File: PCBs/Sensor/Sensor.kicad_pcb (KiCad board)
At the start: 2 copper layers, 35 x 45 mm, 12 parts, among them J1 Conn_01x04_Pin, J2 RJ45, J3 RJ45, J4 RJ45, U1 ATtiny85-20P

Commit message: fixed pcb
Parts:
- JP1: value Jumper_2_Bridged -> Jumper_2_Open; footprint Jumper:SolderJumper-2_P1.3mm_Bridged_RoundedPad1.0x1.5mm -> Jumper:SolderJumper-2_P1.3mm_Open_RoundedPad1.0x1.5mm
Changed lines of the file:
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@@
 		(descr "WR-MJ Modular Jack Horizontal Shielded w. EMI Panel Finger 8P8C Tab Up")
 		(property "Reference" "J3"
-			(at 6.5 -8 90)
+			(at 6.5 -8.5 90)
 			(unlocked yes)
 			(layer "F.SilkS")
 			(effects
 				(font
-					(size 1.1684 1.1684)
-					(thickness 0.1016)
+					(size 1 1)
+					(thickness 0.15)
 				)
 				(justify left bottom)
@@
 		(descr "WR-MJ Modular Jack Horizontal Shielded w. EMI Panel Finger 8P8C Tab Up")
 		(property "Reference" "J4"
-			(at 6.5 -8 -90)
+			(at 6.5 -8.5 270)
 			(unlocked yes)
 			(layer "F.SilkS")
 			(effects
 				(font
-					(size 1.1684 1.1684)
-					(thickness 0.1016)
+					(size 1 1)
+					(thickness 0.15)
 				)
 				(justify left bottom)
@@
 		(descr "WR-MJ Modular Jack Horizontal Shielded w. EMI Panel Finger 8P8C Tab Up")
 		(property "Reference" "J2"
-			(at -8.35 -8 90)
+			(at 6.5 -8.5 90)
 			(unlocked yes)
 			(layer "F.SilkS")
 			(effects
 				(font
-					(size 1.1684 1.1684)
-					(thickness 0.1016)
+					(size 1 1)
+					(thickness 0.15)
 				)
 				(justify left bottom)
@@
 		)
 	)
-	(footprint "Jumper:SolderJumper-2_P1.3mm_Bridged_RoundedPad1.0x1.5mm"
+	(footprint "Jumper:SolderJumper-2_P1.3mm_Open_RoundedPad1.0x1.5mm"
 		(layer "B.Cu")
 		(at 67.15 56.5)
-		(descr "SMD Solder Jumper, 1x1.5mm, rounded Pads, 0.3mm gap, bridged with 1 copper strip")
-		(tags "net tie solder jumper bridged")
+		(descr "SMD Solder Jumper, 1x1.5mm, rounded Pads, 0.3mm gap, open")
+		(tags "solder jumper open")
 		(property "Reference" "JP1"
-			(at 0 1.8 0)
+			(at 0 1.8 180)
 			(layer "B.SilkS")
 			(effects
@@
 			)
 		)
-		(property "Value" "Jumper_2_Bridged"
-			(at 0 -1.9 0)
+		(property "Value" "Jumper_2_Open"
+			(at 0 -1.9 180)
 			(layer "B.Fab")
 			(effects
@@
 			)
 		)
-		(property "Footprint" "Jumper:SolderJumper-2_P1.3mm_Bridged_RoundedPad1.0x1.5mm"
+		(property "Footprint" "Jumper:SolderJumper-2_P1.3mm_Open_RoundedPad1.0x1.5mm"
 			(at 0 0 180)
 			(unlocked yes)
@@
 			)
 		)
-		(property "Description" "Jumper, 2-pole, closed/bridged"
+		(property "Description" "Jumper, 2-pole, open"
 			(at 0 0 180)
 			(unlocked yes)
@@
 		(zone_connect 1)
 		(attr exclude_from_pos_files)
-		(net_tie_pad_groups "1, 2")
-		(fp_poly
-			(pts
-				(xy 0.25 0.3) (xy -0.25 0.3) (xy -0.25 -0.3) (xy 0.25 -0.3)
-			)
-			(stroke
-				(width 0)
-				(type solid)
-			)
-			(fill solid)
-			(layer "B.Cu")
-		)
 		(fp_line
 			(start -1.4 0.3)
@@
 	(via
 		(at 70 64.5)
-		(size 0.6)
+		(size 0.7)
 		(drill 0.3)
 		(layers "F.Cu" "B.Cu")
@@
 	(via
 		(at 57 66.5)
-		(size 0.6)
+		(size 0.7)
 		(drill 0.3)
 		(layers "F.Cu" "B.Cu")
@@
 	(via
 		(at 83 65.5)
-		(size 0.6)
+		(size 0.7)
 		(drill 0.3)
 		(layers "F.Cu" "B.Cu")
@@
 	(via
 		(at 80 83.5)
-		(size 0.6)
+		(size 0.7)
 		(drill 0.3)
 		(layers "F.Cu" "B.Cu")
@@
 	(via
 		(at 80 88.5)
-		(size 0.6)
+		(size 0.7)
 		(drill 0.3)
 		(layers "F.Cu" "B.Cu")
@@
 	(via
 		(at 74 71)
-		(size 0.6)
+		(size 0.7)
 		(drill 0.3)
 		(layers "F.Cu" "B.Cu")
@@
 	(via
 		(at 84 67.5)
-		(size 0.6)
+		(size 0.7)
 		(drill 0.3)
 		(layers "F.Cu" "B.Cu")
@@
 	(via
 		(at 71 71)
-		(size 0.6)
+		(size 0.7)
 		(drill 0.3)
 		(layers "F.Cu" "B.Cu")
@@
 	(via
 		(at 71 77)
-		(size 0.6)
+		(size 0.7)
 		(drill 0.3)
 		(layers "F.Cu" "B.Cu")
@@
 	(via
 		(at 71 66.5)
-		(size 0.6)
+		(size 0.7)
 		(drill 0.3)
 		(layers "F.Cu" "B.Cu")
@@
 	(via
 		(at 73 77)
-		(size 0.6)
+		(size 0.7)
 		(drill 0.3)
 		(layers "F.Cu" "B.Cu")
@@
 	(via
 		(at 61.5 68)
-		(size 0.6)
+		(size 0.7)
 		(drill 0.3)
 		(layers "F.Cu" "B.Cu")
@@
 	(via
 		(at 72 82.5)
-		(size 0.6)
+		(size 0.7)
 		(drill 0.3)
 		(layers "F.Cu" "B.Cu")

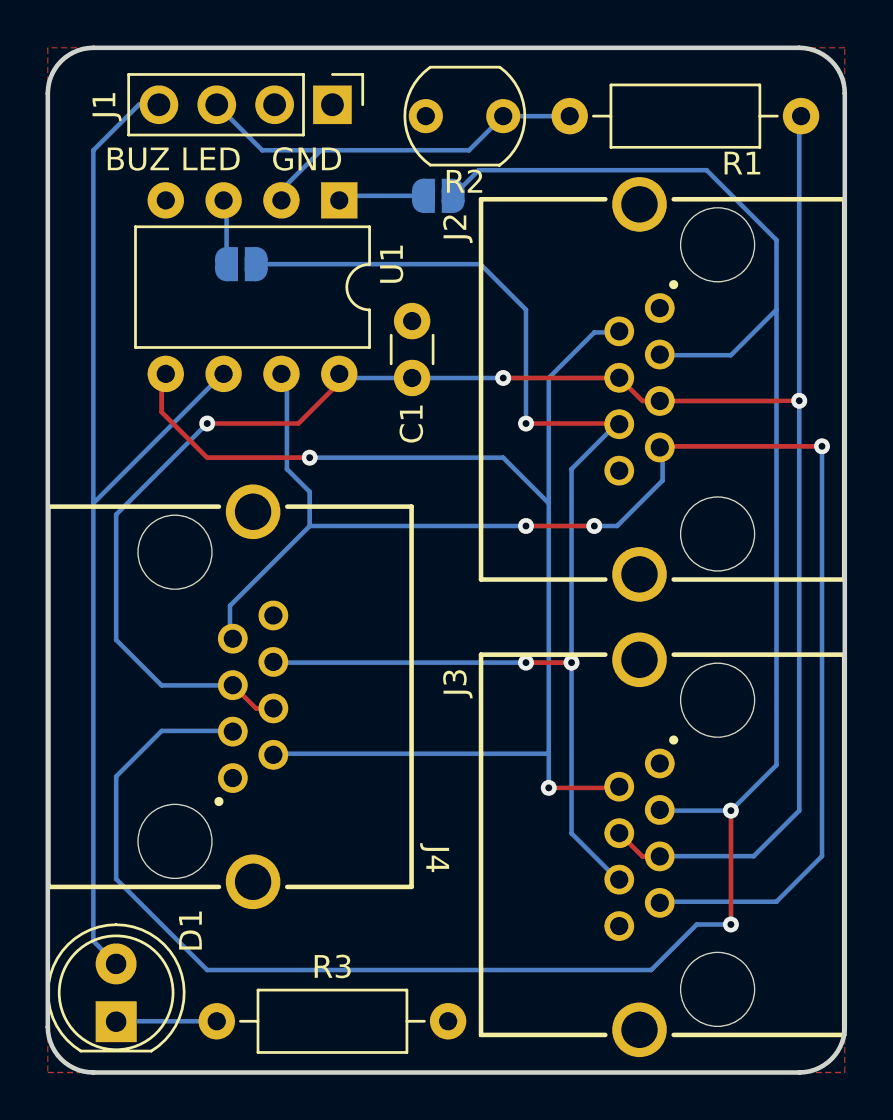
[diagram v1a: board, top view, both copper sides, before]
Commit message: wider traces
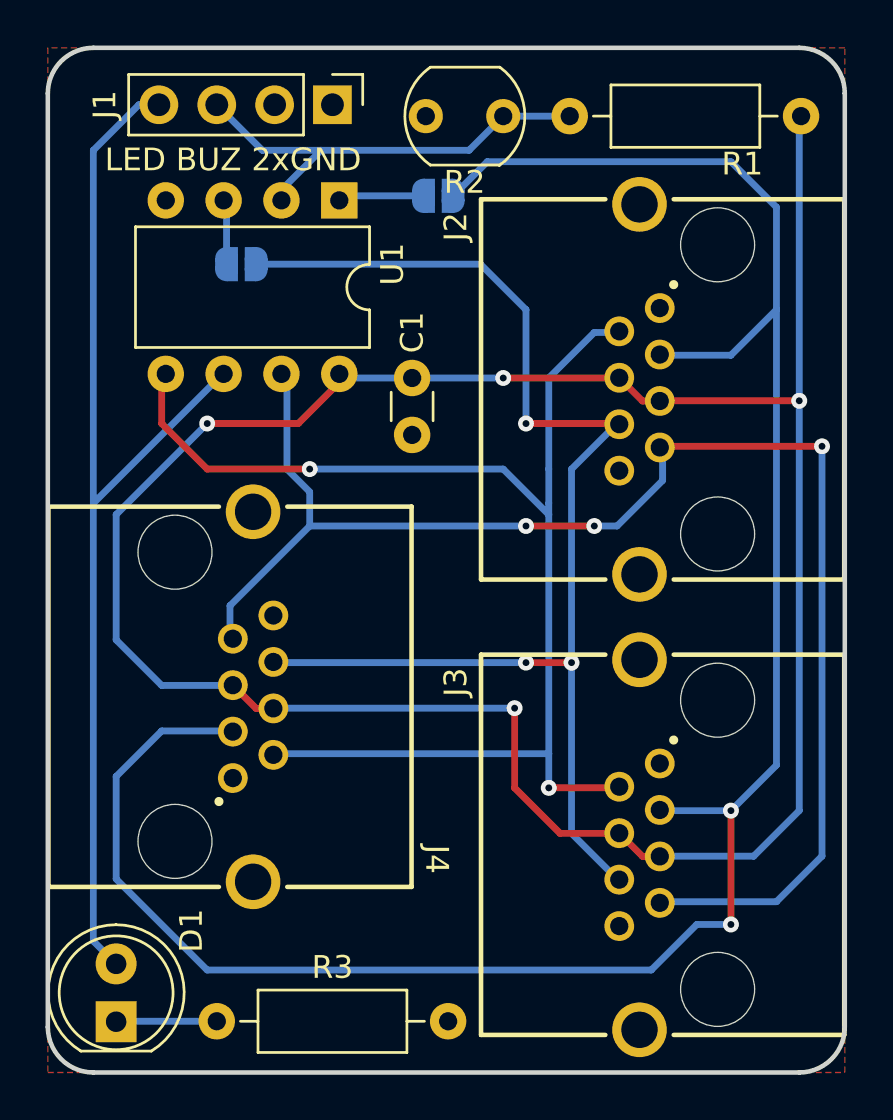
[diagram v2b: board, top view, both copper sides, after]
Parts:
- turned C1 to -90 degrees
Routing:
- net +3.3V: track 86.9 -> 106.5 mm, vias 3 -> 4
- net Net-(JP1-B): track 95.9 -> 97.0 mm
- net /SDA0: track 57.6 -> 58.1 mm
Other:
- board text added: "LED BUZ 2xGND"
- board text added: "Laser-Parkour Sensor Rev. 02 © 2024 Manuel König HHN HTWG x42.space"
- board text removed: "BUZ LED GND"
- board text removed: "Laser-Parkour Sensor Rev. 01 © 2024 Manuel König HHN HTWG x42.space"
